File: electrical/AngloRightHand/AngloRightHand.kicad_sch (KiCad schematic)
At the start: 49 parts, among them J3 TC2030-NL, U1 DRV5053VAQDBZR, U10 DRV5053VAQDBZR, U11 DRV5053VAQDBZR, U12 DRV5053VAQDBZR, U13 DRV5053VAQDBZR, U14 DRV5053VAQDBZR, U15 DRV5053VAQDBZR, U16 STM32L072CBTx, U17 CD74HC4067SM, U2 DRV5053VAQDBZR, U3 DRV5053VAQDBZR, U4 DRV5053VAQDBZR, U5 DRV5053VAQDBZR, U6 DRV5053VAQDBZR, U7 DRV5053VAQDBZR, U8 DRV5053VAQDBZR, U9 DRV5053VAQDBZR

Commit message: PCB adjustments
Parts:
- H1, H2: footprint MountingHole:MountingHole_3.2mm_M3_Pad -> MountingHole:MountingHole_3.2mm_M3; symbol Mechanical:MountingHole_Pad -> Mechanical:MountingHole
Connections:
- net GND: no longer H1.1, H2.1
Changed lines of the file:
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@@
 	(symbol
 		(lib_id "power:GND")
-		(at 116.84 232.41 0)
-		(unit 1)
-		(exclude_from_sim no)
-		(in_bom yes)
-		(on_board yes)
-		(dnp no)
-		(fields_autoplaced yes)
-		(property "Reference" "#PWR0118"
-			(at 116.84 238.76 0)
-			(effects
-				(font
-					(size 1.27 1.27)
-				)
-				(hide yes)
-			)
-		)
-		(property "Value" "GND"
-			(at 116.84 237.49 0)
-			(effects
-				(font
-					(size 1.27 1.27)
-				)
-				(hide yes)
-			)
-		)
-		(property "Footprint" ""
-			(at 116.84 232.41 0)
-			(effects
-				(font
-					(size 1.27 1.27)
-				)
-				(hide yes)
-			)
-		)
-		(property "Datasheet" ""
-			(at 116.84 232.41 0)
-			(effects
-				(font
-					(size 1.27 1.27)
-				)
-				(hide yes)
-			)
-		)
-		(property "Description" "Power symbol creates a global label with name \"GND\" , ground"
-			(at 116.84 232.41 0)
-			(effects
-				(font
-					(size 1.27 1.27)
-				)
-				(hide yes)
-			)
-		)
-		(pin "1"
-		)
-		(instances
-			(project "AngloRightHand"
-				(path "/da26d94e-7a50-4b99-9678-5aaaf6987a15"
-					(reference "#PWR0118")
-					(unit 1)
-				)
-			)
-		)
-	)
-	(symbol
-		(lib_id "power:GND")
 		(at 106.68 198.12 0)
 		(unit 1)
@@
 	)
 	(symbol
-		(lib_id "Mechanical:MountingHole_Pad")
+		(lib_id "Mechanical:MountingHole")
 		(at 96.52 229.87 0)
 		(unit 1)
@@
 			)
 		)
-		(property "Footprint" "MountingHole:MountingHole_3.2mm_M3_Pad"
+		(property "Footprint" "MountingHole:MountingHole_3.2mm_M3"
 			(at 96.52 229.87 0)
 			(effects
@@
 			)
 		)
-		(property "Description" "Mounting Hole with connection"
+		(property "Description" "Mounting Hole without connection"
 			(at 96.52 229.87 0)
 			(effects
@@
 			)
 		)
-		(pin "1"
-		)
 		(instances
 			(project "control"
@@
 	)
 	(symbol
-		(lib_id "power:GND")
-		(at 96.52 232.41 0)
-		(unit 1)
-		(exclude_from_sim no)
-		(in_bom yes)
-		(on_board yes)
-		(dnp no)
-		(fields_autoplaced yes)
-		(property "Reference" "#PWR0117"
-			(at 96.52 238.76 0)
-			(effects
-				(font
-					(size 1.27 1.27)
-				)
-				(hide yes)
-			)
-		)
-		(property "Value" "GND"
-			(at 96.52 237.49 0)
-			(effects
-				(font
-					(size 1.27 1.27)
-				)
-				(hide yes)
-			)
-		)
-		(property "Footprint" ""
-			(at 96.52 232.41 0)
-			(effects
-				(font
-					(size 1.27 1.27)
-				)
-				(hide yes)
-			)
-		)
-		(property "Datasheet" ""
-			(at 96.52 232.41 0)
-			(effects
-				(font
-					(size 1.27 1.27)
-				)
-				(hide yes)
-			)
-		)
-		(property "Description" "Power symbol creates a global label with name \"GND\" , ground"
-			(at 96.52 232.41 0)
-			(effects
-				(font
-					(size 1.27 1.27)
-				)
-				(hide yes)
-			)
-		)
-		(pin "1"
-		)
-		(instances
-			(project "control"
-				(path "/da26d94e-7a50-4b99-9678-5aaaf6987a15"
-					(reference "#PWR0117")
-					(unit 1)
-				)
-			)
-		)
-	)
-	(symbol
 		(lib_id "MidiConcertina:TI_DRV5053xDBZ")
 		(at 340.36 125.73 0)
@@
 	)
 	(symbol
-		(lib_id "Mechanical:MountingHole_Pad")
+		(lib_id "Mechanical:MountingHole")
 		(at 116.84 229.87 0)
 		(unit 1)
@@
 			)
 		)
-		(property "Footprint" "MountingHole:MountingHole_3.2mm_M3_Pad"
+		(property "Footprint" "MountingHole:MountingHole_3.2mm_M3"
 			(at 116.84 229.87 0)
 			(effects
@@
 			)
 		)
-		(property "Description" "Mounting Hole with connection"
+		(property "Description" "Mounting Hole without connection"
 			(at 116.84 229.87 0)
 			(effects
@@
 			)
 		)
-		(pin "1"
-		)
 		(instances

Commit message: Add licenses
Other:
- company: Bushel Basket Musical Instruments -> (none)
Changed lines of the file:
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@@
 	(title_block
 		(title "MIDI Concertina Controller")
-		(company "Bushel Basket Musical Instruments")
+		(comment 1 "https://ohwr.org/cern_ohl_s_v2.pdf")
+		(comment 2 "Licensed under CERN-OHL-S v2 or any later version")
+		(comment 3 "Copyright 2025 Steven Schulteis")
 	)
 	(junction

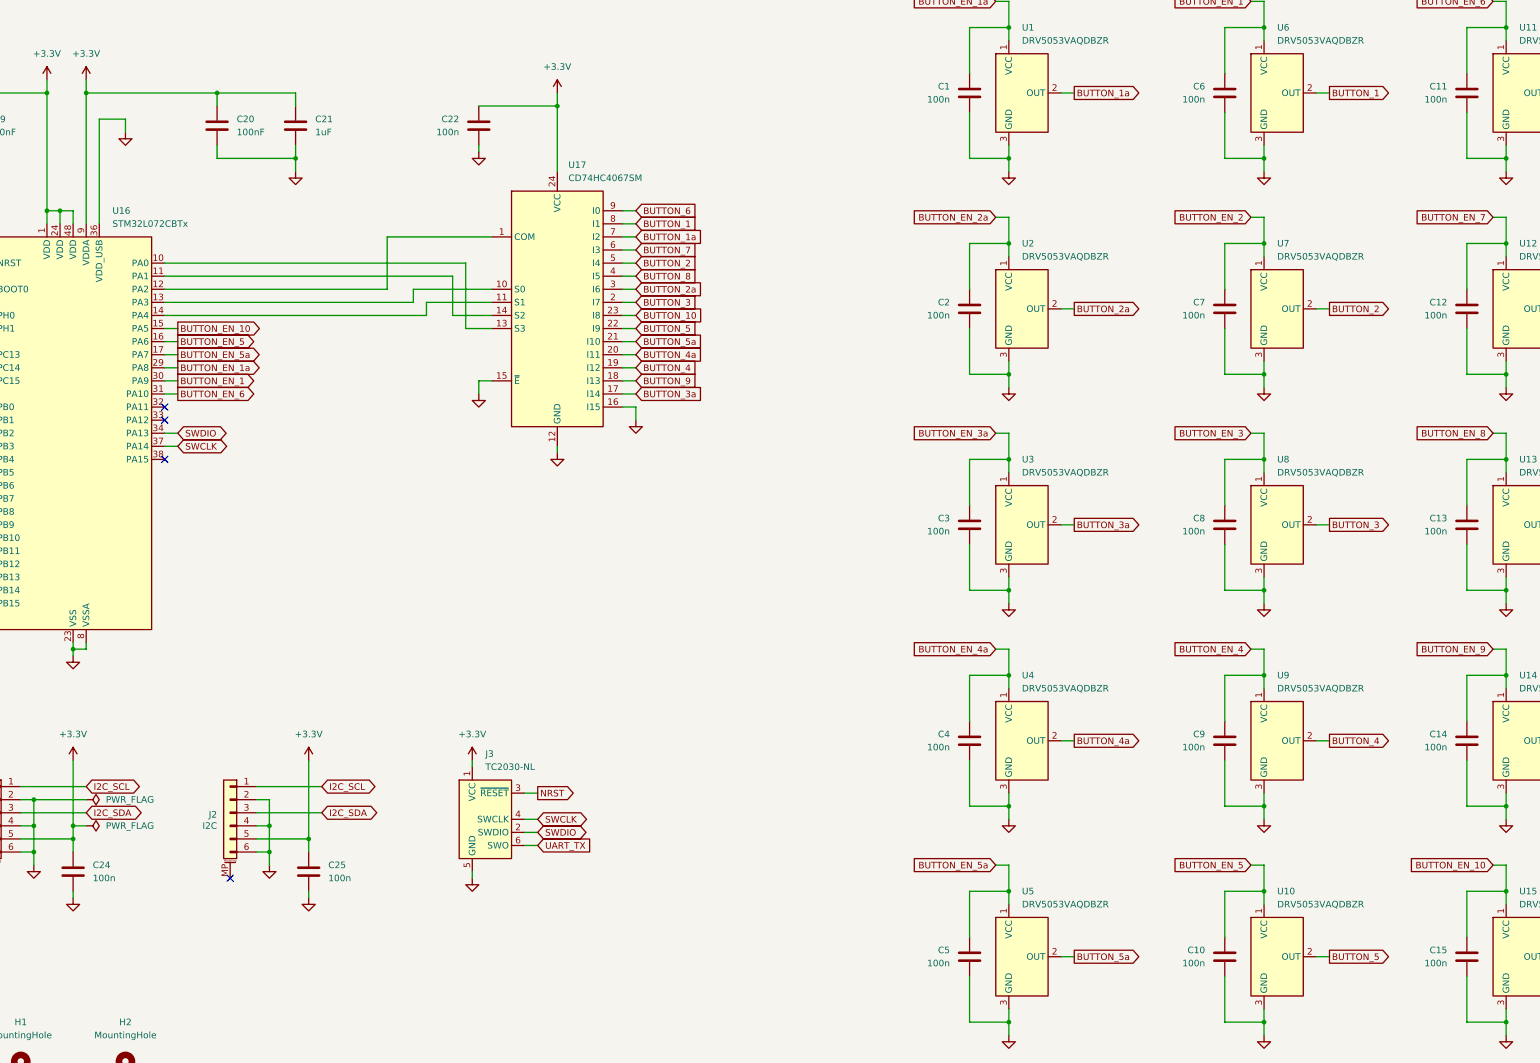
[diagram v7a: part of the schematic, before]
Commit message: Minor corrections to right hand board
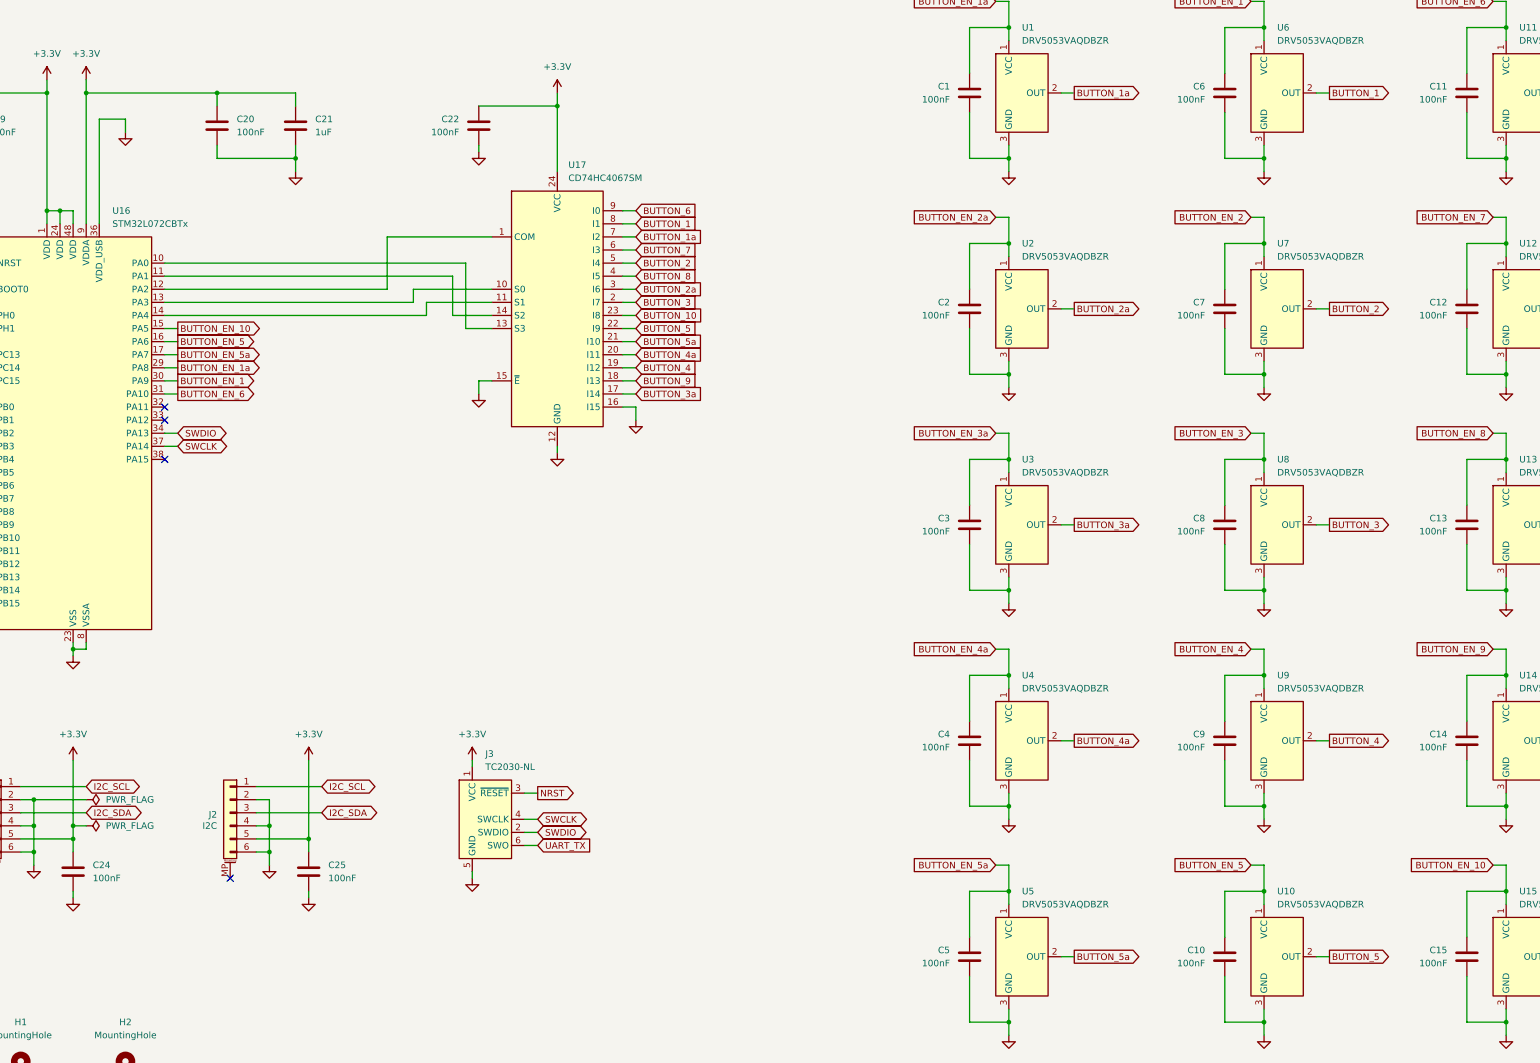
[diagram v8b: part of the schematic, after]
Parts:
- C1, C10, C11, C12, C13, C14, C15, C2, C22, C24, C25, C3, C4, C5, C6, C7, C8, C9: value 100n -> 100nF
- J1, J2: LCSC C99277 -> C17393620
